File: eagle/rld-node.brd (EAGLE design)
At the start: 50 x 40 mm, 30 parts

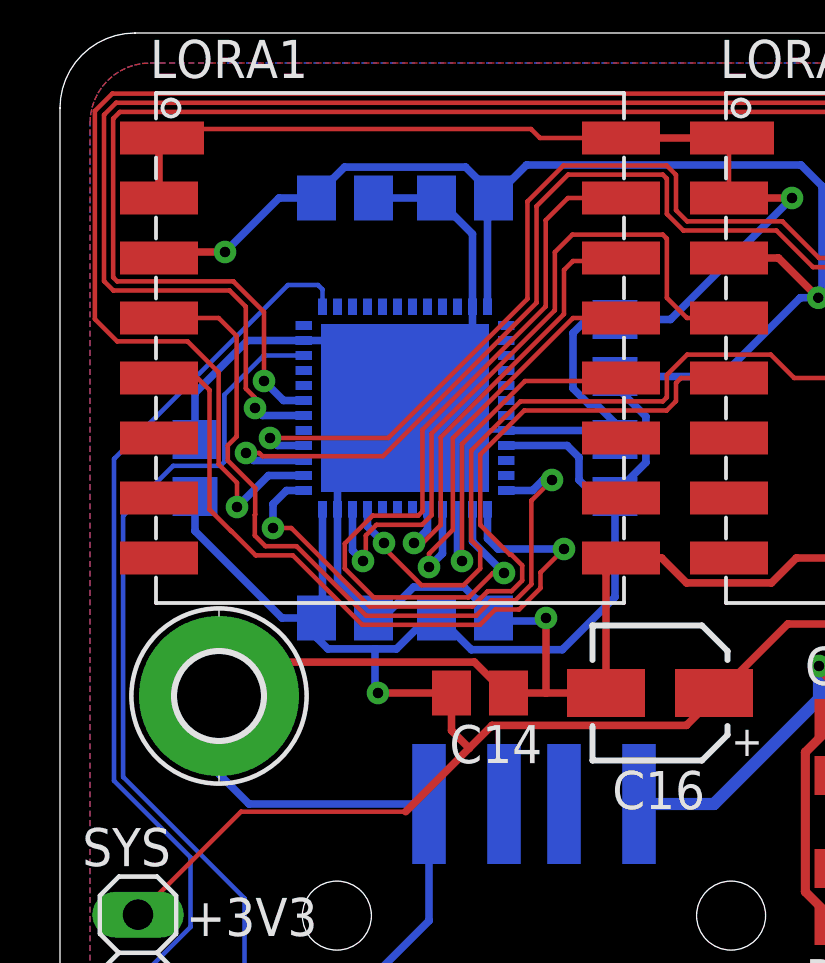
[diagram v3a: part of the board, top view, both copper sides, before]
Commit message: Fixed missing voltage trace and fixed floating BOOT and NRST
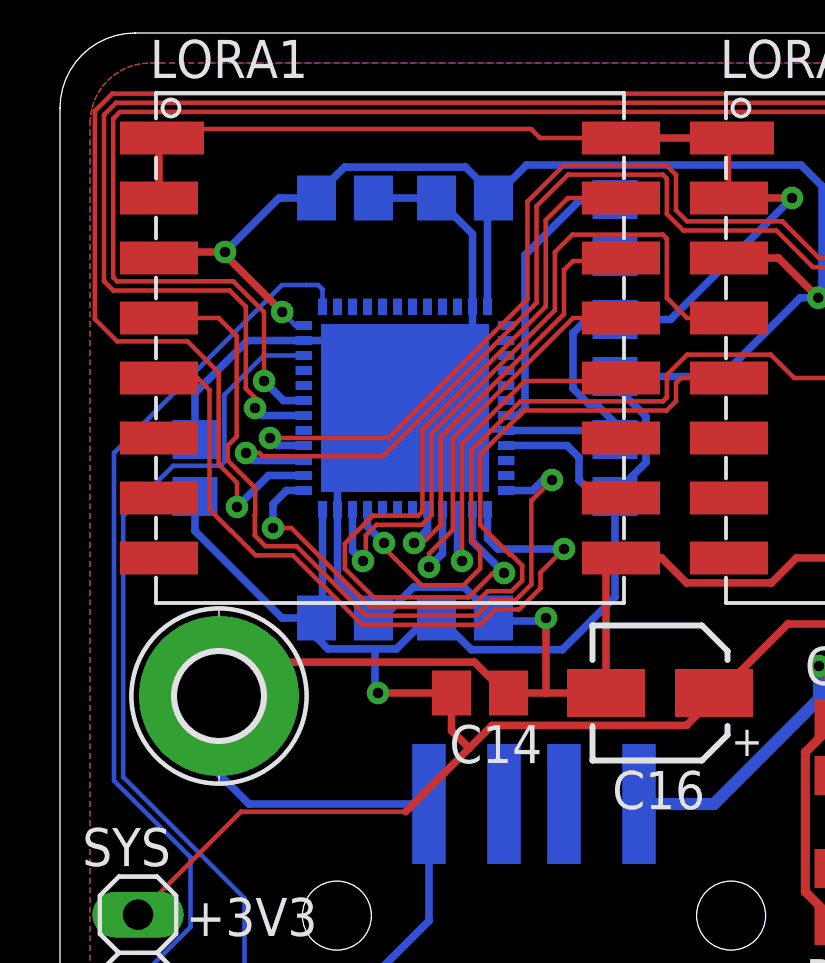
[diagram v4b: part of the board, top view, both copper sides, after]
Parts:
- added C15: 4.7uF, rcl:C0805
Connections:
- new net N$8: C15.1, U$5.7
- net +3V3: now also U$5.36
- net GND: now also C15.2, U$5.44
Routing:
- net N$8: track 0.00 -> 9.59 mm
- net +3V3: track 145.7 -> 149.4 mm, vias 3 -> 4
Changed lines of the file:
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@@
 <grid distance="0.1" unitdist="mm" unit="mm" style="lines" multiple="1" display="no" altdistance="0.05" altunitdist="mm" altunit="mm"/>
 <layers>
-<layer number="1" name="Top" color="4" fill="1" visible="yes" active="yes"/>
+<layer number="1" name="Top" color="4" fill="1" visible="no" active="yes"/>
 <layer number="2" name="Route2" color="16" fill="1" visible="no" active="no"/>
 <layer number="3" name="Route3" color="17" fill="1" visible="no" active="no"/>
@@
 <layer number="19" name="Unrouted" color="6" fill="1" visible="yes" active="yes"/>
 <layer number="20" name="Dimension" color="24" fill="1" visible="yes" active="yes"/>
-<layer number="21" name="tPlace" color="7" fill="1" visible="yes" active="yes"/>
-<layer number="22" name="bPlace" color="7" fill="1" visible="no" active="yes"/>
-<layer number="23" name="tOrigins" color="15" fill="1" visible="yes" active="yes"/>
-<layer number="24" name="bOrigins" color="15" fill="1" visible="no" active="yes"/>
-<layer number="25" name="tNames" color="7" fill="1" visible="yes" active="yes"/>
-<layer number="26" name="bNames" color="7" fill="1" visible="no" active="yes"/>
+<layer number="21" name="tPlace" color="7" fill="1" visible="no" active="yes"/>
+<layer number="22" name="bPlace" color="7" fill="1" visible="yes" active="yes"/>
+<layer number="23" name="tOrigins" color="15" fill="1" visible="no" active="yes"/>
+<layer number="24" name="bOrigins" color="15" fill="1" visible="yes" active="yes"/>
+<layer number="25" name="tNames" color="7" fill="1" visible="no" active="yes"/>
+<layer number="26" name="bNames" color="7" fill="1" visible="yes" active="yes"/>
 <layer number="27" name="tValues" color="7" fill="1" visible="no" active="yes"/>
 <layer number="28" name="bValues" color="7" fill="1" visible="no" active="yes"/>
@@
 <layer number="37" name="tTest" color="7" fill="1" visible="no" active="yes"/>
 <layer number="38" name="bTest" color="7" fill="1" visible="no" active="yes"/>
-<layer number="39" name="tKeepout" color="4" fill="11" visible="yes" active="yes"/>
-<layer number="40" name="bKeepout" color="1" fill="11" visible="no" active="yes"/>
-<layer number="41" name="tRestrict" color="4" fill="10" visible="yes" active="yes"/>
-<layer number="42" name="bRestrict" color="1" fill="10" visible="no" active="yes"/>
+<layer number="39" name="tKeepout" color="4" fill="11" visible="no" active="yes"/>
+<layer number="40" name="bKeepout" color="1" fill="11" visible="yes" active="yes"/>
+<layer number="41" name="tRestrict" color="4" fill="10" visible="no" active="yes"/>
+<layer number="42" name="bRestrict" color="1" fill="10" visible="yes" active="yes"/>
 <layer number="43" name="vRestrict" color="2" fill="10" visible="no" active="yes"/>
 <layer number="44" name="Drills" color="7" fill="1" visible="no" active="yes"/>
-<layer number="45" name="Holes" color="7" fill="1" visible="yes" active="yes"/>
+<layer number="45" name="Holes" color="7" fill="1" visible="no" active="yes"/>
 <layer number="46" name="Milling" color="3" fill="1" visible="no" active="yes"/>
 <layer number="47" name="Measures" color="7" fill="1" visible="no" active="yes"/>
@@
 <layer number="49" name="Reference" color="7" fill="1" visible="no" active="yes"/>
 <layer number="50" name="dxf" color="7" fill="1" visible="no" active="no"/>
-<layer number="51" name="tDocu" color="7" fill="1" visible="yes" active="yes"/>
-<layer number="52" name="bDocu" color="7" fill="1" visible="no" active="yes"/>
+<layer number="51" name="tDocu" color="7" fill="1" visible="no" active="yes"/>
+<layer number="52" name="bDocu" color="7" fill="1" visible="yes" active="yes"/>
 <layer number="53" name="tGND_GNDA" color="7" fill="1" visible="no" active="no"/>
 <layer number="54" name="bGND_GNDA" color="7" fill="1" visible="no" active="no"/>
@@
 <attribute name="POPULARITY" value="6" x="5.3" y="17.9" size="1.778" layer="27" display="off"/>
 </element>
+<element name="C15" library="rcl" library_urn="urn:adsk.eagle:library:334" package="C0805" package3d_urn="urn:adsk.eagle:package:23617/2" value="4.7uF" x="18.5" y="33.5" smashed="yes" rot="MR270">
+<attribute name="NAME" x="17.23" y="34.77" size="1.27" layer="26" rot="MR270"/>
+<attribute name="POPULARITY" value="88" x="18.5" y="33.5" size="1.778" layer="28" rot="MR270" display="off"/>
+<attribute name="SPICEPREFIX" value="C" x="18.5" y="33.5" size="1.778" layer="28" rot="MR270" display="off"/>
+<attribute name="VALUE" x="21.04" y="34.77" size="1.27" layer="28" rot="MR270"/>
+</element>
 </elements>
 <signals>
@@
 <wire x1="17.63426875" y1="27.6206" x2="17.1" y2="28.15486875" width="0.254" layer="16"/>
 <wire x1="17.1" y1="28.15486875" x2="17.1" y2="30" width="0.254" layer="16"/>
+<contactref element="U$5" pad="44"/>
+<contactref element="C15" pad="2"/>
 </signal>
 <signal name="N$1">
@@
 <wire x1="13.5206" y1="35.5294" x2="14.45" y2="34.6" width="0.254" layer="16"/>
 <wire x1="3.3" y1="32.5" x2="3.5" y2="32.7" width="0.254" layer="1"/>
-<wire x1="5.5" y1="32.7" x2="3.5" y2="32.7" width="0.254" layer="1"/>
+<wire x1="5.5" y1="32.7" x2="5.4" y2="32.7" width="0.254" layer="1"/>
 <via x="5.5" y="32.7" extent="1-16" drill="0.35"/>
+<wire x1="5.4" y1="32.7" x2="3.5" y2="32.7" width="0.254" layer="1"/>
 <wire x1="8.55" y1="34.5" x2="7.3" y2="34.5" width="0.254" layer="16"/>
 <wire x1="7.3" y1="34.5" x2="5.5" y2="32.7" width="0.254" layer="16"/>
@@
 <wire x1="17.3" y1="25.1" x2="17.74513125" y2="24.65486875" width="0.254" layer="16"/>
 <wire x1="17.74513125" y1="24.65486875" x2="18.5" y2="24.65486875" width="0.254" layer="16"/>
+<contactref element="U$5" pad="36"/>
+<wire x1="8.125" y1="30.25" x2="7.85" y2="30.25" width="0.1524" layer="16"/>
+<wire x1="7.85" y1="30.25" x2="7.4" y2="30.7" width="0.1524" layer="16"/>
+<wire x1="7.4" y1="30.7" x2="7.4068" y2="30.7" width="0.1524" layer="16"/>
+<via x="7.4068" y="30.7" extent="1-16" drill="0.35"/>
+<wire x1="7.4068" y1="30.7" x2="5.4068" y2="32.7" width="0.254" layer="1"/>
+<wire x1="5.4068" y1="32.7" x2="5.4" y2="32.7" width="0.1524" layer="1"/>
 </signal>
 <signal name="N$5">
@@
 <wire x1="8.75" y1="30.875" x2="8.75" y2="31.45" width="0.1524" layer="16"/>
 <wire x1="8.75" y1="31.45" x2="8.6" y2="31.6" width="0.1524" layer="16"/>
-<wire x1="7.5971" y1="31.6" x2="8.6" y2="31.6" width="0.1524" layer="16"/>
-<wire x1="1.7996" y1="25.8025" x2="7.5971" y2="31.6" width="0.1524" layer="16"/>
+<wire x1="7.3971" y1="31.6" x2="8.2" y2="31.6" width="0.1524" layer="16"/>
+<wire x1="8.2" y1="31.6" x2="8.6" y2="31.6" width="0.1524" layer="16"/>
+<wire x1="1.7996" y1="26.0025" x2="6.89855" y2="31.10145" width="0.1524" layer="16"/>
+<wire x1="6.89855" y1="31.10145" x2="7.3971" y2="31.6" width="0.1524" layer="16"/>
 <wire x1="2.6" y1="8.07" x2="2.6" y2="8.447075" width="0.1524" layer="16"/>
 <wire x1="2.6" y1="8.447075" x2="4.3526" y2="10.199675" width="0.1524" layer="16"/>
-<wire x1="1.7996" y1="15.07434375" x2="1.7996" y2="25.8025" width="0.1524" layer="16"/>
+<wire x1="1.7996" y1="15.07434375" x2="1.7996" y2="26.0025" width="0.1524" layer="16"/>
 <wire x1="4.3526" y1="10.199675" x2="4.3526" y2="12.52134375" width="0.1524" layer="16"/>
 <wire x1="4.3526" y1="12.52134375" x2="1.7996" y2="15.07434375" width="0.1524" layer="16"/>
@@
 <wire x1="40.946675" y1="37.9796" x2="1.7442" y2="37.9796" width="0.1524" layer="1"/>
 </signal>
+<signal name="N$8">
+<contactref element="U$5" pad="7"/>
+<contactref element="C15" pad="1"/>
+<wire x1="15.5" y1="27.5" x2="15.25" y2="27.25" width="0.254" layer="16"/>
+<wire x1="15.25" y1="27.25" x2="14.875" y2="27.25" width="0.254" layer="16"/>
+<wire x1="18.5" y1="34.45" x2="18.45" y2="34.4" width="0.254" layer="16"/>
+<wire x1="18.45" y1="34.4" x2="17.3" y2="34.4" width="0.254" layer="16"/>
+<wire x1="17.3" y1="34.4" x2="15.5" y2="32.6" width="0.254" layer="16"/>
+<wire x1="15.5" y1="32.6" x2="15.5" y2="27.5" width="0.254" layer="16"/>
+</signal>
 </signals>

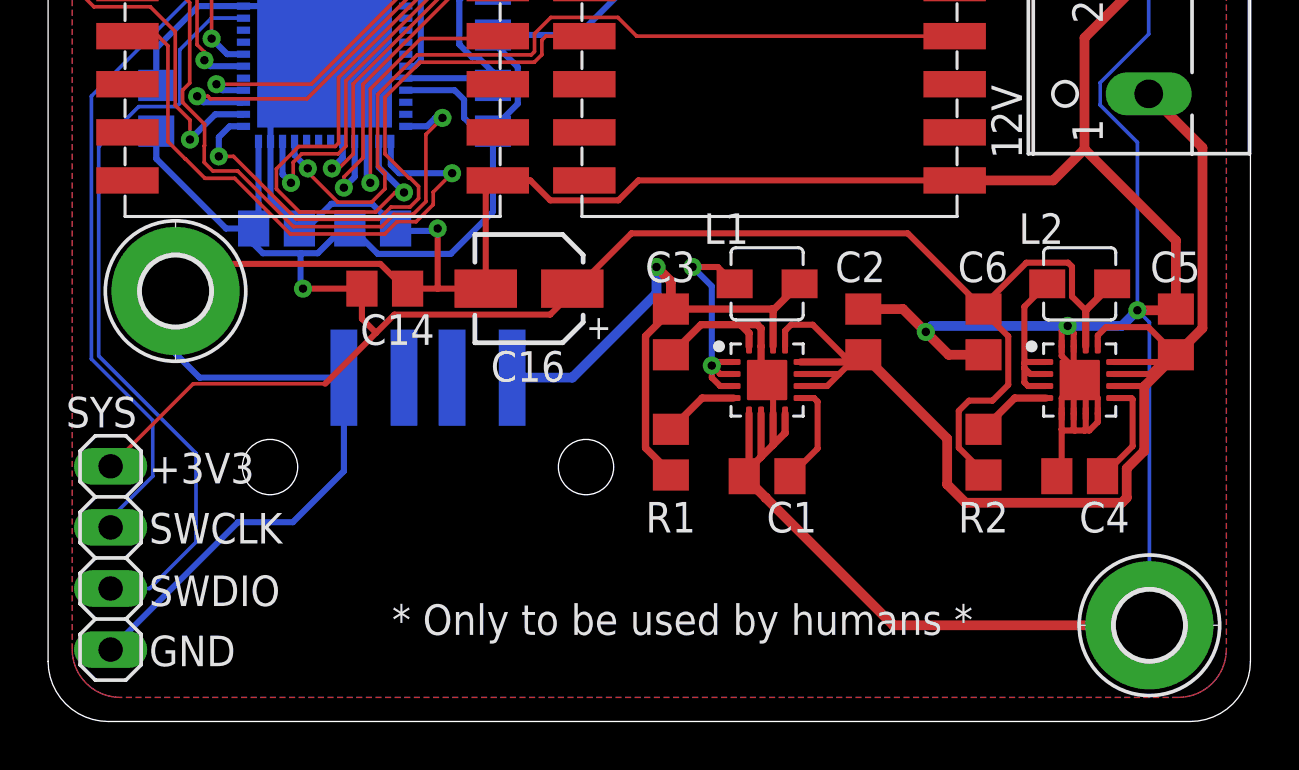
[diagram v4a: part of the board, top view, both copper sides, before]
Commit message: Changed USB socket and added power LED
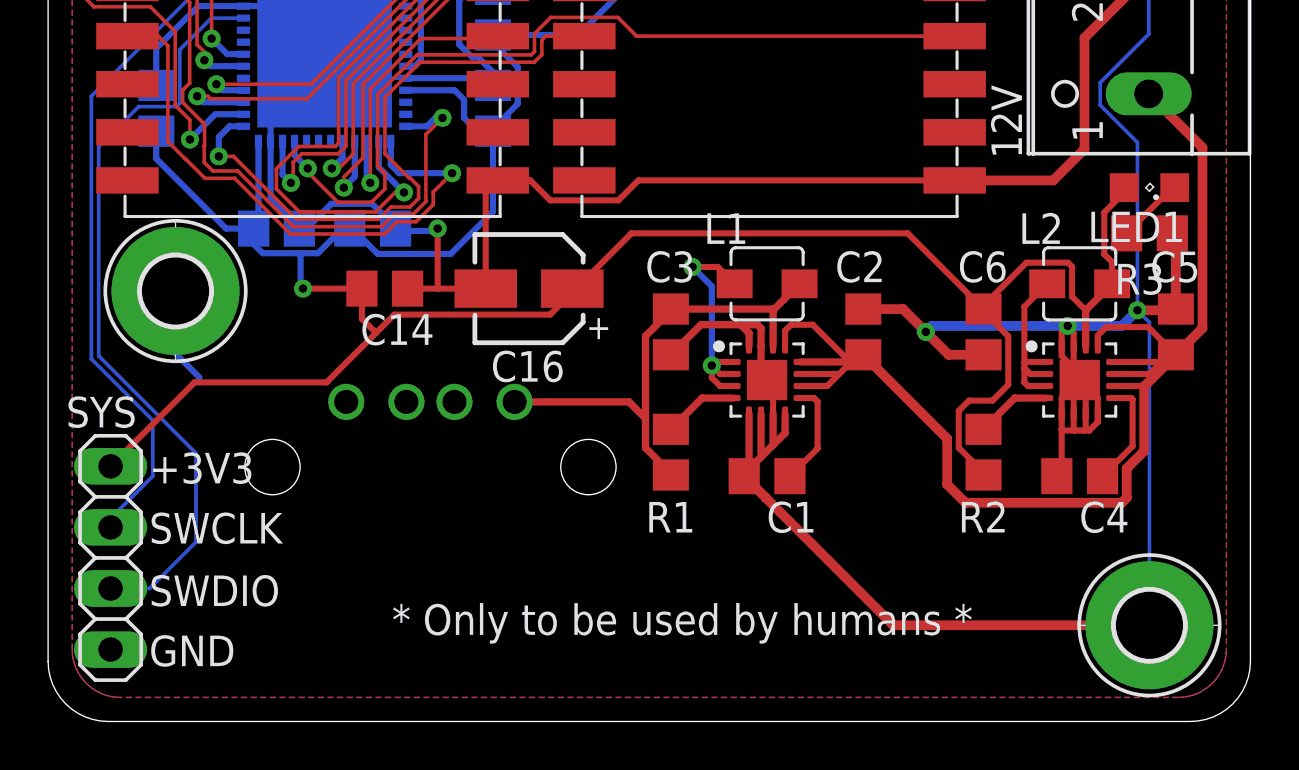
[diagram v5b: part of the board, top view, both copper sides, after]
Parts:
- removed X2: (no value), con-yamaichi:USB-A003
- added LED1: (no value), led:SML0805
- added R3: (no value), rcl:R0805
- added X3: (no value), con-amp:USB
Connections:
- new net N$7: LED1.C, R3.2
- net +3V3: now also LED1.A
- net +5V: now also X3.1; no longer X2.1
- net GND: now also R3.1, X3.4; no longer X2.4
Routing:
- net GND: track 291.0 -> 254.1 mm
- net +3V3: track 149.4 -> 154.6 mm
- net +5V: track 25.6 -> 20.8 mm, vias 1 -> 0
- net N$7: track 0.00 -> 2.79 mm
